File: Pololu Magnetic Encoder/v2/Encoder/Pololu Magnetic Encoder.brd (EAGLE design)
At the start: 17.8 x 11.7 mm, 8 parts, among them U1 AS5035

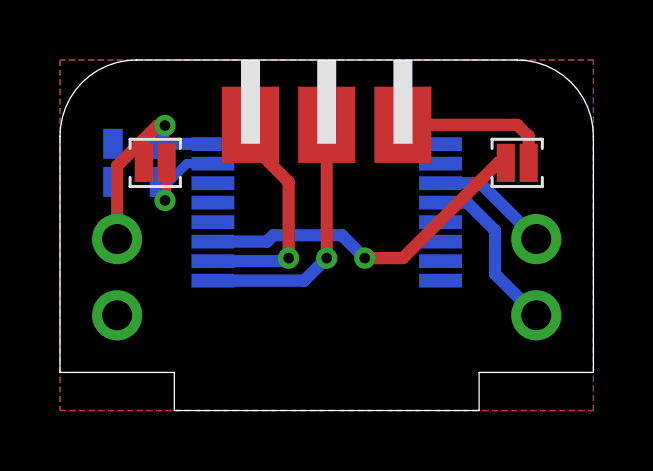
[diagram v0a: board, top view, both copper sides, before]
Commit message: Updated Pololu Magnetic Encoder, fixing pullup issue and adding new silkscreen info
Signed-off-by: Cruz Monrreal II <Cruz.Monrreal@gmail.com>
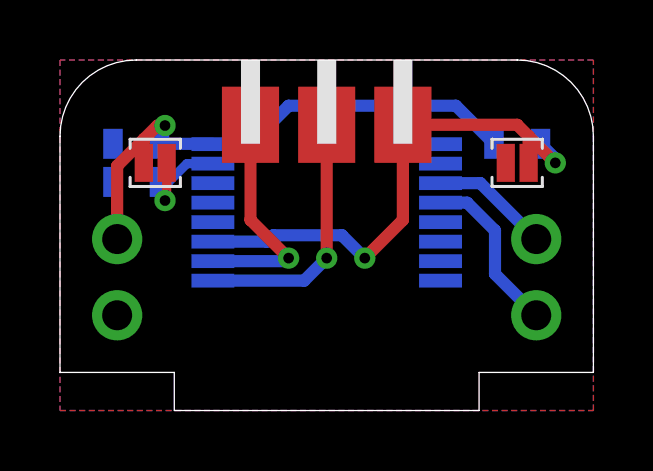
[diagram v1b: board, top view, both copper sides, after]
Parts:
- added R1: 100k, .standardparts:0603
- turned J2 to 0 degrees
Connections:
- removed net N$1: J2.2, U1.11
- net !CS: now also J2.2, R1.2, U1.11; no longer J2.1
- net GND: now also J2.1
- net VIN: now also R1.1
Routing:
- net !CS: track 5.24 -> 17.8 mm, vias 0 -> 2
- net N$1: track 11.5 -> 0.00 mm, vias 1 -> 0
- net VIN: track 7.85 -> 18.3 mm
- net CLK: track 7.54 -> 8.17 mm
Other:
- board text added: "innovativemaker.com"
- board text removed: "24-Jun-2012"
- board text removed: "ThinkMakeTest"
